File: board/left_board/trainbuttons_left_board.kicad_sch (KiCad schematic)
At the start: 5 parts, among them J101 USB_C_Receptacle_USB2.0_16P, J102 HDMI_A, J301 HDMI_A

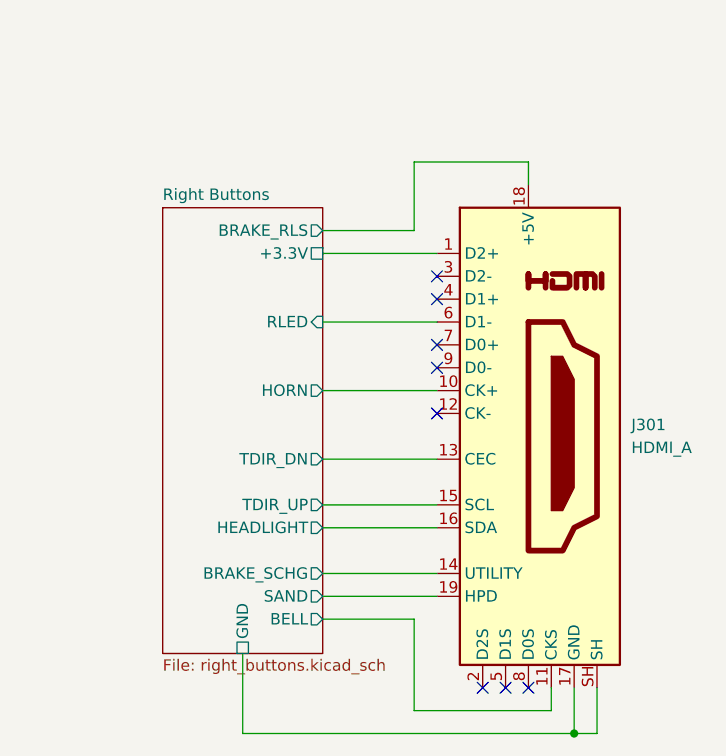
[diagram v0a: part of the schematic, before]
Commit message: split board into left and right
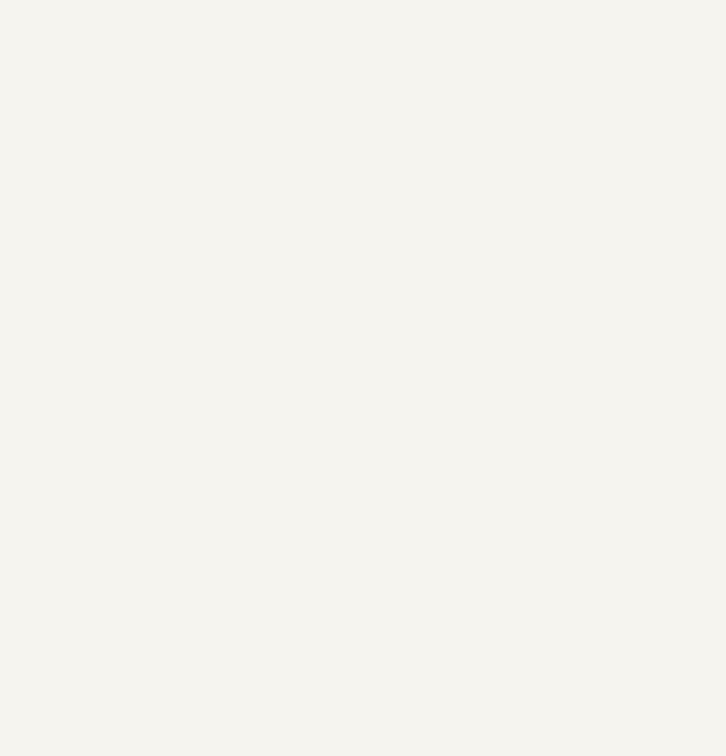
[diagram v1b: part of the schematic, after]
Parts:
- removed J301: HDMI_A, Connector_HDMI:HDMI_A_Molex_208658-1001_Horizontal, symbol Connector:HDMI_A
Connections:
- no-connect marks 18 -> 10
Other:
- removed sheet Right Buttons
